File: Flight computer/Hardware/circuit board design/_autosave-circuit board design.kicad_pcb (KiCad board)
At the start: 4 copper layers, 30.5 x 82.6 mm, 89 parts, among them J1 Conn_01x05, J2 USB_B_Micro, J3 Screw_Terminal_01x04, J4 Conn_01x02, J5 Screw_Terminal_01x04, J6 Conn_Coaxial, J7 Conn_Coaxial, U1 IIS2MDC, U10 BMI088, U11 ATSAML21J18B-AUT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

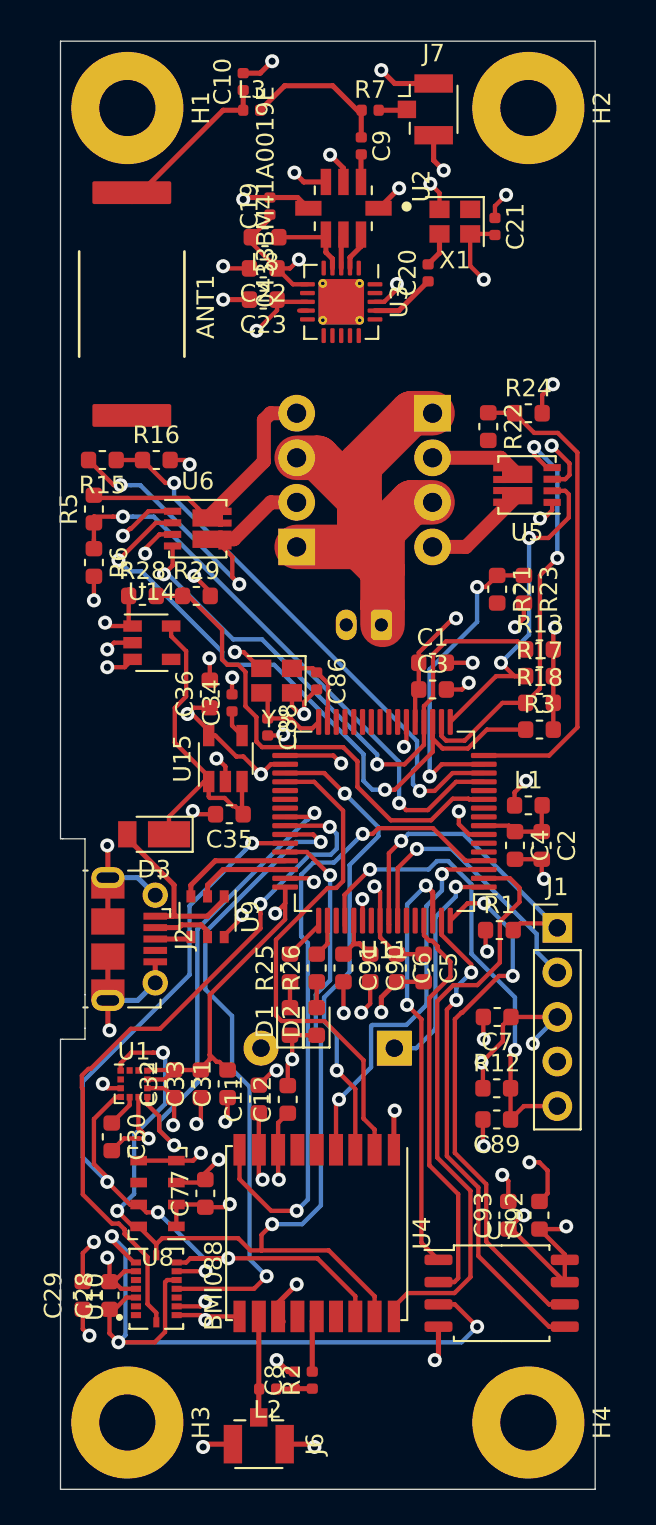
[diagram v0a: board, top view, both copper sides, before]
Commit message: added in crystal footprint
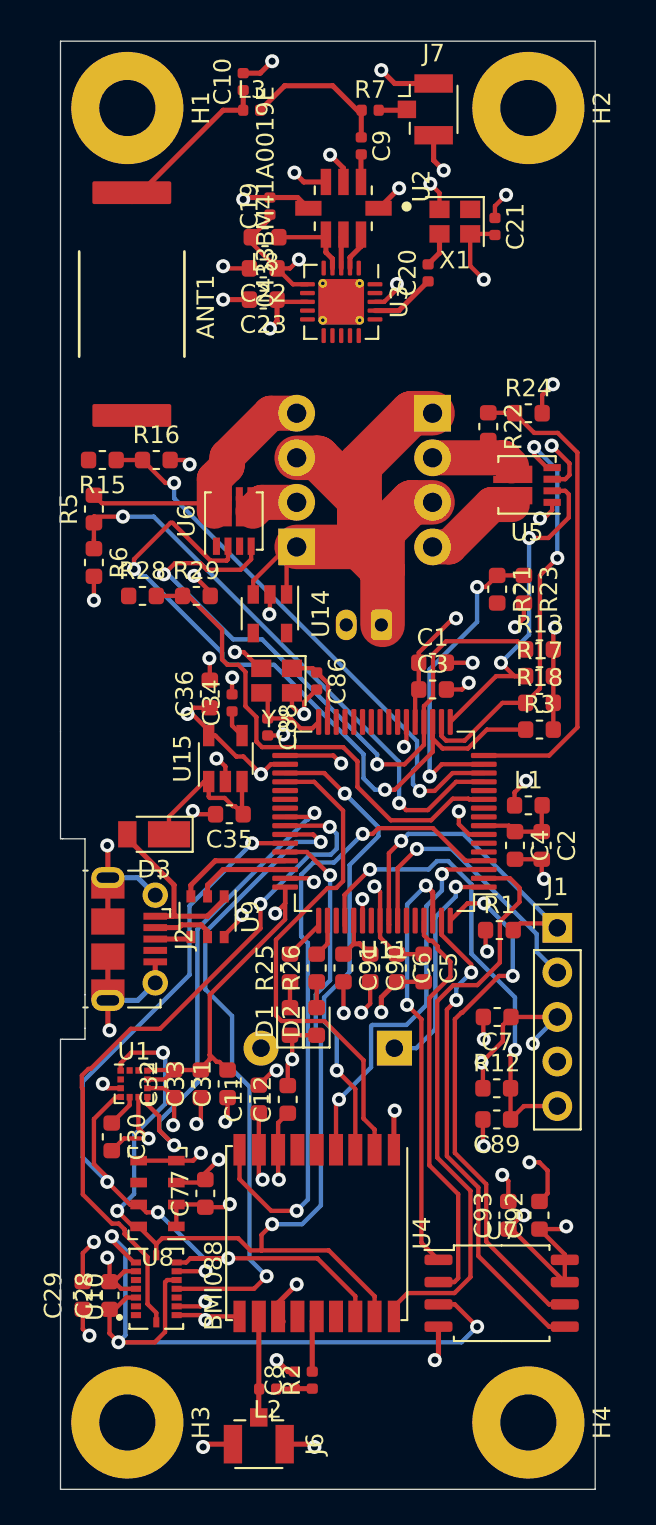
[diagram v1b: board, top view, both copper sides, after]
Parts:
- Y3: footprint Crystal:Crystal_SMD_2520-4Pin_2.5x2.0mm -> flight-computer:Crystal_SMD_2520-4Pin_2.5x2.0mm
- moved U14 6.93 mm to (104.3, 90.4), turned to 270 degrees
- moved U6 2.10 mm to (102.2, 85.1), turned to 90 degrees
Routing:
- net +3V3: track 307.6 -> 285.9 mm
- net /pyro_driver/FET_B: track 19.9 -> 2.71 mm, vias 2 -> 0
- net Vdrive: track 65.1 -> 76.4 mm, vias 2 -> 0
- net Net-(C35-Pad1): track 19.5 -> 9.52 mm
- net GND: track 159.0 -> 152.9 mm, vias 66 -> 64
- net /pyro_driver/FIRE_B: track 33.1 -> 37.6 mm
- net /pyro_driver/FIRE_A: track 38.4 -> 41.7 mm
- net /pyro_driver/FET_D: track 5.22 -> 4.69 mm
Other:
- net class FETs added: clearance 0.2, trace_width 2, via_dia 0.8, via_drill 0.4
